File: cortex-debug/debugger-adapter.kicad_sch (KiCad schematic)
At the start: 4 parts

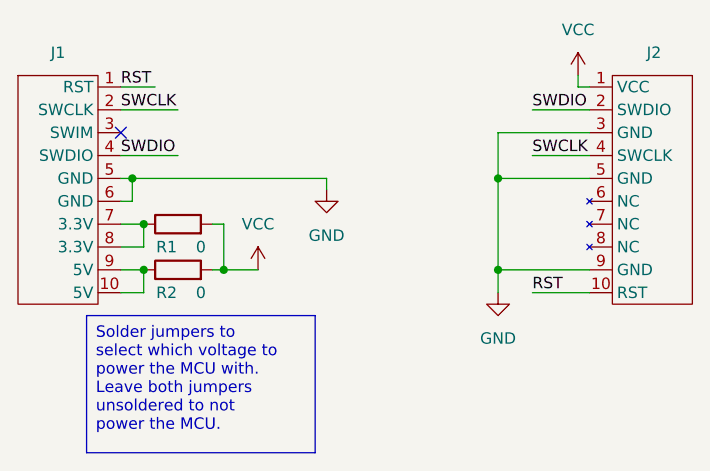
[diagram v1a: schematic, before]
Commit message: Replace solder jumpers with selector switch
I got annoyed that my debugger was set for the wrong
voltage or set to provide power when I didn't want it to, so
small revision to add a selector switch. Makes the board a little bigger
but whatever.
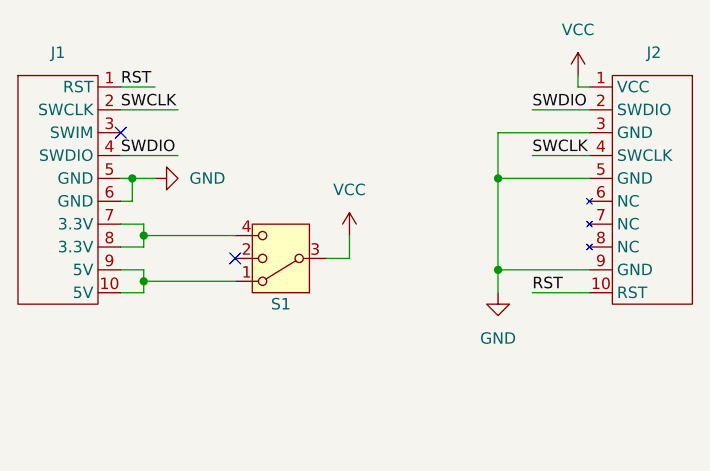
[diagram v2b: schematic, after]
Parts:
- removed R1, R2: 0, Resistor_SMD:R_0805_2012Metric_Pad1.20x1.40mm_HandSolder, symbol Device:R
- added S1: ~, common-components:Slide_SP3T, symbol common-components:Slide_SP3T
- J1: Digikey Part Number (none) -> S9194-ND; Manufacturer Part Number (none) -> SFH11-PBPC-D05-ST-BK
- J2: Digikey Part Number (none) -> 1175-1664-ND; Manufacturer Part Number (none) -> 3240-10-00
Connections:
- net VCC: now also S1.3
- net at J1.10 (5V), J1.9 (5V): now also S1.1
- net at J1.7 (3.3V), J1.8 (3.3V): now also S1.4
- no-connect marks 1 -> 2
